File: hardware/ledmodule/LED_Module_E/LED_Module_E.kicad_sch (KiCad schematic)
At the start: 92 parts, among them J1 SFW20S-2STE1LF, J3 009159008603906, Q1 Si3456DDV, Q11 Si3456DDV, Q12 Si3456DDV, Q2 Si3456DDV, Q3 Si3456DDV, Q4 Si3456DDV, Q5 Si3456DDV, Q6 Si3456DDV, Q7 Si3456DDV, Q8 Si3456DDV, U1 TMP1075DGK, U2 74HCT244, U3 24AA02UIDT-I/OT

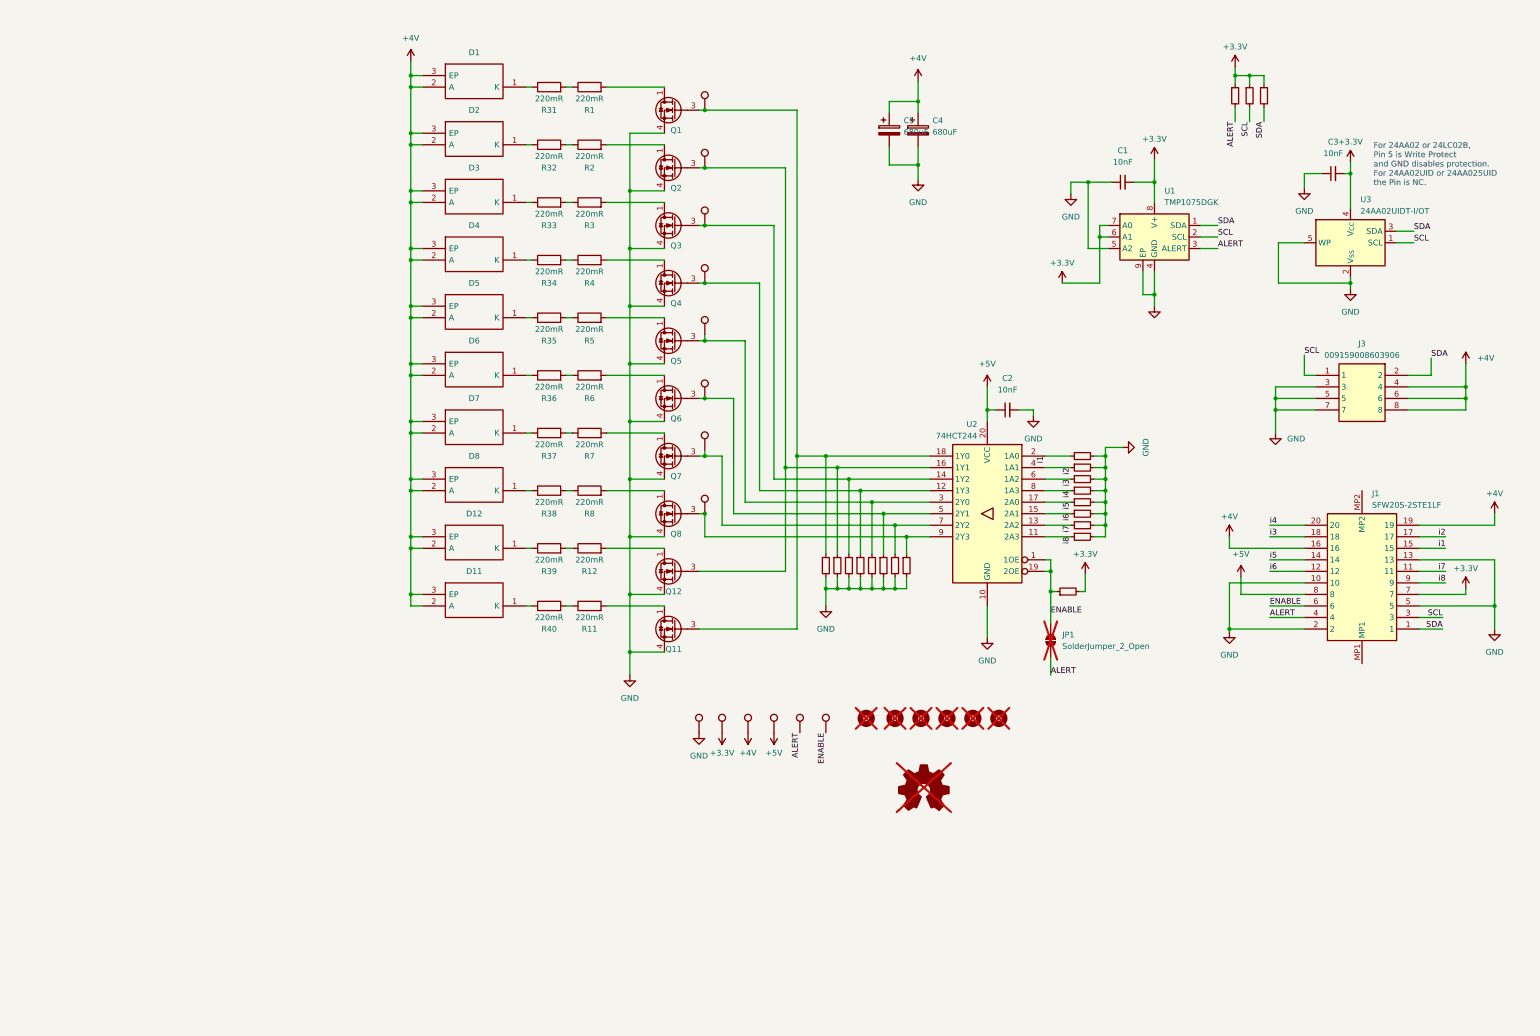
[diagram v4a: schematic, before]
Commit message: Latest versions of all five PCBs that make up the ABL, maybe ready for prototype production.
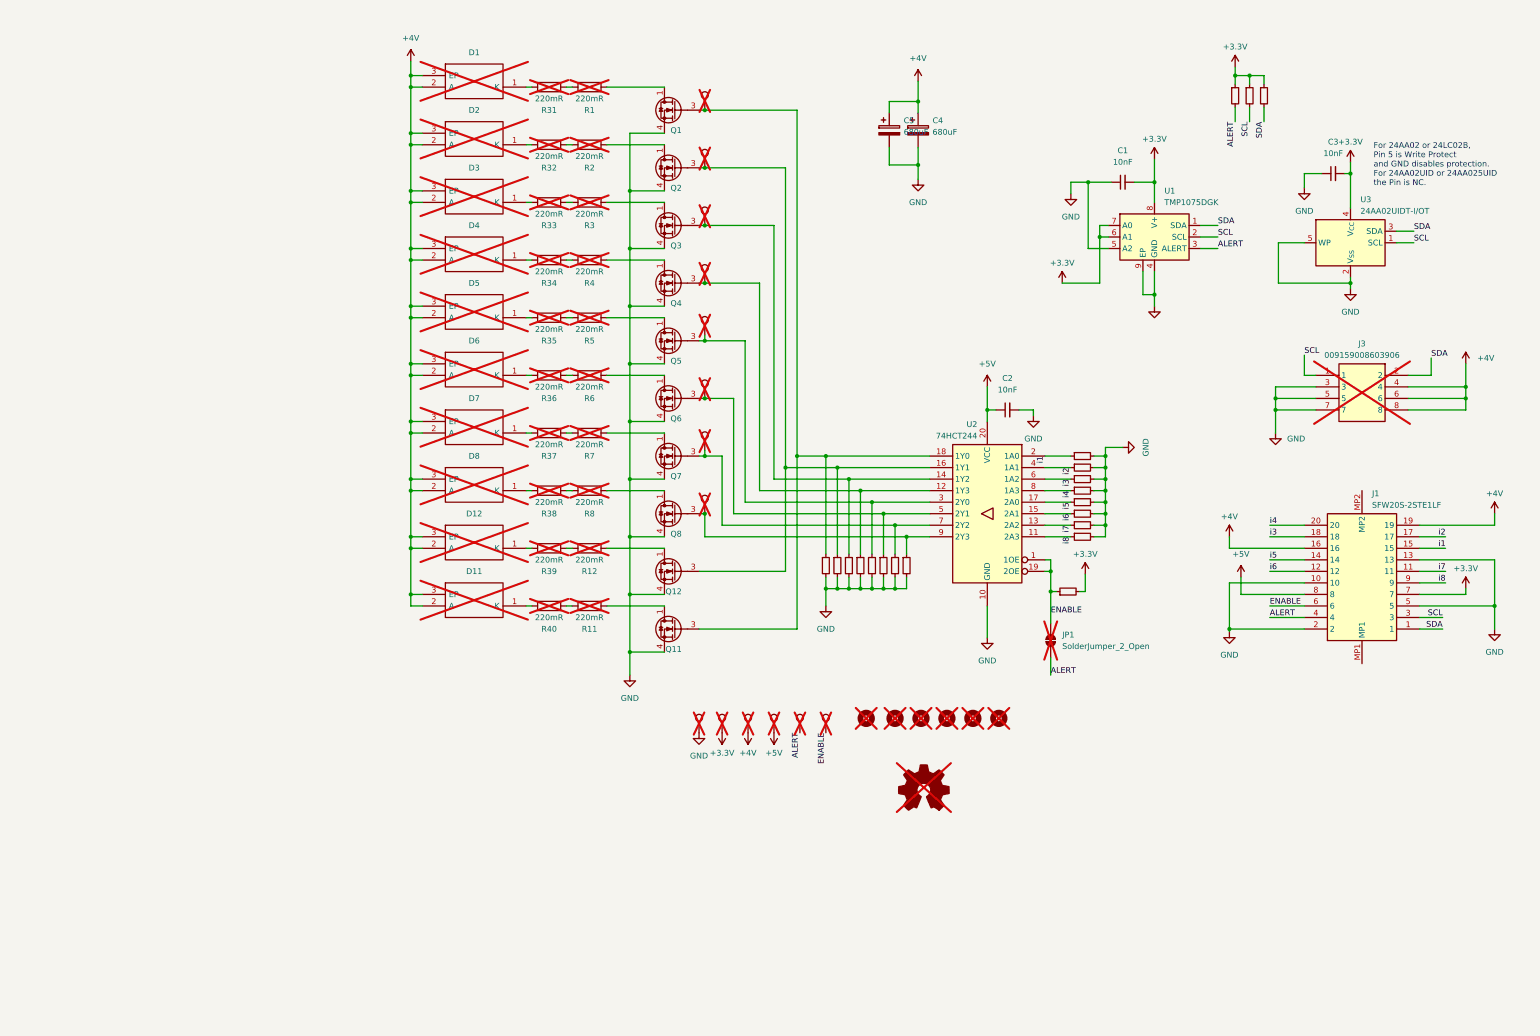
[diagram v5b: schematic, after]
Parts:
- C1: LCSC Part # (none) -> C15195; Manufacturer_Part_Number (none) -> CL05B103KB5NNNC
- C2, C3: LCSC Part # (none) -> C57112; Manufacturer_Part_Number (none) -> 0603B103K500NT
- C4, C5: LCSC Part # (none) -> C2760485; Manufacturer_Part_Number (none) -> RVT1A681M0810 680UF 10V
- D1, D11, D12, D2, D3, D4, D5, D6, D7, D8, J3, R1, R11, R12, R2, R3, R31, R32, R33, R34, R35, R36, R37, R38, R39, R4, R40, R5, R6, R7, R8, TP1, TP10, TP11, TP12, TP13, TP14, TP2, TP3, TP4, TP5, TP6, TP7, TP8, TP9: now not fitted
- J1: LCSC Part # (none) -> C5407823
- Q1, Q11, Q12, Q2, Q3, Q4, Q5, Q6, Q7, Q8: LCSC Part # (none) -> C145273; Manufacturer_Part_Number (none) -> SI3456DDV-T1-GE3
- R10, R13, R14, R15, R16, R17, R18, R19, R20, R21, R22, R23, R24, R25, R26, R27, R28, R29, R30, R9: LCSC Part # (none) -> C13167; Manufacturer_Part_Number (none) -> 0603WAF2701T5E
- U1: footprint Package_SON:WSON-8-1EP_2x2mm_P0.5mm_EP0.9x1.6mm_ThermalVias -> Package_SO:VSSOP-8_3.0x3.0mm_P0.65mm; LCSC Part # (none) -> C2864807; Manufacturer_Part_Number (none) -> TMP1075DGKR
- U2: LCSC Part # (none) -> C5978; Manufacturer_Part_Number (none) -> SI3456DDV-T1-GE3
- U3: LCSC Part # (none) -> C511274; Manufacturer_Part_Number (none) -> 24AA02UIDT-I/OT

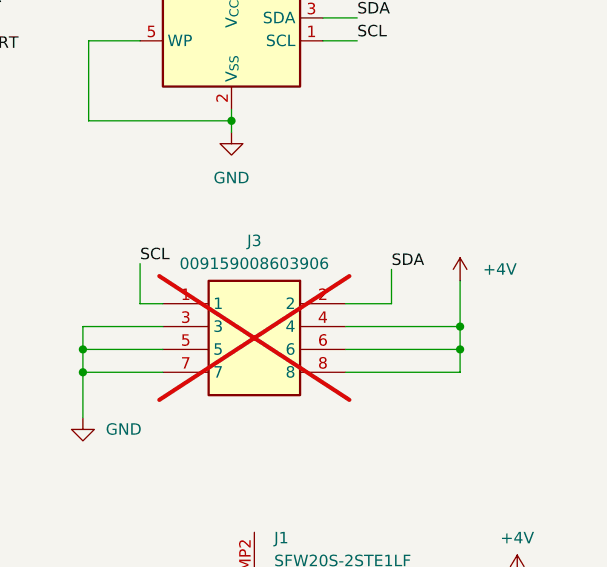
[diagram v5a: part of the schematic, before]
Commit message: Clean up schematics and minor fixes in PCB layouts.
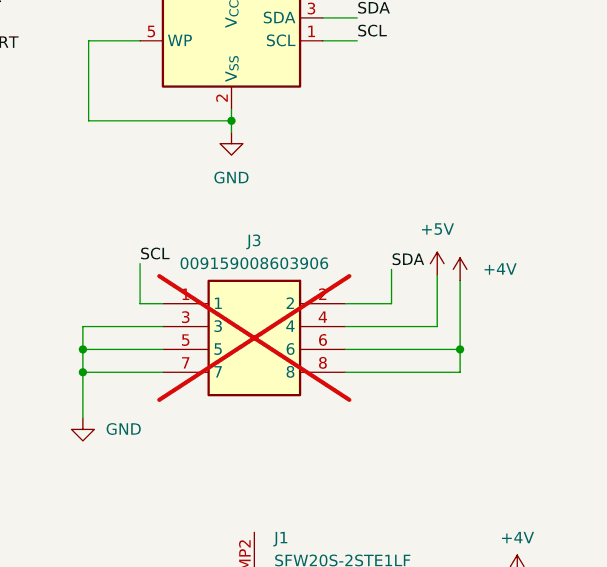
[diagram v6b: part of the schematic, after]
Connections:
- net +4V: no longer J3.4
- net +5V: now also J3.4
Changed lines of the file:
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@@
 	)
 	(junction
-		(at 269.24 93.98)
-		(diameter 0)
-		(color 0 0 0 0)
-	)
-	(junction
 		(at 36.83 76.2)
 		(diameter 0)
@@
 	(wire
 		(pts
-			(xy 269.24 93.98) (xy 269.24 88.9)
-		)
-		(stroke
-			(width 0)
-			(type default)
-		)
-	)
-	(wire
-		(pts
 			(xy 259.08 127) (xy 264.795 127)
 		)
@@
 	(wire
 		(pts
-			(xy 269.24 93.98) (xy 269.24 96.52)
+			(xy 269.24 88.9) (xy 269.24 96.52)
 		)
 		(stroke
@@
 	(wire
 		(pts
+			(xy 266.7 93.98) (xy 256.54 93.98)
+		)
+		(stroke
+			(width 0)
+			(type default)
+		)
+	)
+	(wire
+		(pts
 			(xy 101.6 83.82) (xy 110.49 83.82)
 		)
@@
 	(wire
 		(pts
-			(xy 256.54 93.98) (xy 269.24 93.98)
-		)
-		(stroke
-			(width 0)
-			(type default)
-		)
-	)
-	(wire
-		(pts
 			(xy 105.41 124.46) (xy 105.41 109.22)
 		)
@@
 	(wire
 		(pts
+			(xy 266.7 88.265) (xy 266.7 93.98)
+		)
+		(stroke
+			(width 0)
+			(type default)
+		)
+	)
+	(wire
+		(pts
 			(xy 100.33 58.42) (xy 101.6 58.42)
 		)
@@
 					(unit 1)
 				)
+			)
+		)
+	)
+	(symbol
+		(lib_id "power:+5V")
+		(at 266.7 88.265 0)
+		(unit 1)
+		(exclude_from_sim no)
+		(in_bom yes)
+		(on_board yes)
+		(dnp no)
+		(fields_autoplaced yes)
+		(property "Reference" "#PWR03"
+			(at 266.7 92.075 0)
+			(effects
+				(font
+					(size 1.27 1.27)
+				)
+				(hide yes)
+			)
+		)
+		(property "Value" "+5V"
+			(at 266.7 83.185 0)
+			(effects
+				(font
+					(size 1.27 1.27)
+				)
+			)
+		)
+		(property "Footprint" ""
+			(at 266.7 88.265 0)
+			(effects
+				(font
+					(size 1.27 1.27)
+				)
+				(hide yes)
+			)
+		)
+		(property "Datasheet" ""
+			(at 266.7 88.265 0)
+			(effects
+				(font
+					(size 1.27 1.27)
+				)
+				(hide yes)
+			)
+		)
+		(property "Description" "Power symbol creates a global label with name \"+5V\""
+			(at 266.7 88.265 0)
+			(effects
+				(font
+					(size 1.27 1.27)
+				)
+				(hide yes)
+			)
+		)
+		(pin "1"
+		)
+		(instances
+			(project "LED_Module_E"
+				(path "/271a71a9-d0cc-4466-ad75-113fb931f3c8"
+					(reference "#PWR03")
+					(unit 1)
+				)
